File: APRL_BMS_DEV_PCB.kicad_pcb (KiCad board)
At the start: 4 copper layers, 2 parts, among them U1 BQ756506-Q1, U2 STM32F446RCTx

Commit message: Edited PCB a little
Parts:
- added C1: 1u, Capacitor_SMD:C_0603_1608Metric, F.Cu at (80.2, 61.4)
- added C10: 10n, Capacitor_SMD:C_0603_1608Metric, F.Cu at (80.2, 84.0)
- added C11: 1u, Capacitor_SMD:C_0603_1608Metric, F.Cu at (84.2, 61.4)
- added C12: 4.7u, Capacitor_SMD:C_0603_1608Metric, F.Cu at (84.2, 63.9)
- added C13: 20n, Capacitor_SMD:C_0603_1608Metric, F.Cu at (84.2, 66.5)
- added C14: .47u, Capacitor_SMD:C_0603_1608Metric, F.Cu at (84.2, 69.0)
- added C15: 0.1u, Capacitor_SMD:C_0603_1608Metric, F.Cu at (84.2, 71.5)
- added C16: 0.2u, Capacitor_SMD:C_0603_1608Metric, F.Cu at (134.7, 44.5)
- added C17: .56u, Capacitor_SMD:C_0603_1608Metric, F.Cu at (84.2, 74.0)
- added C18: 10u, Capacitor_SMD:C_0603_1608Metric, F.Cu at (84.2, 76.5)
- added C19: 1.5u, Capacitor_SMD:C_0603_1608Metric, F.Cu at (134.7, 47.0)
- added C2: 100n, Capacitor_SMD:C_0603_1608Metric, F.Cu at (80.2, 63.9)
- added C20: 1.5u, Capacitor_SMD:C_0603_1608Metric, F.Cu at (134.7, 49.5)
- added C21: 1.5u, Capacitor_SMD:C_0603_1608Metric, F.Cu at (134.7, 52.0)
- added C22: 1.5u, Capacitor_SMD:C_0603_1608Metric, F.Cu at (134.7, 54.5)
- added C23: 1.5u, Capacitor_SMD:C_0603_1608Metric, F.Cu at (134.7, 57.0)
- added C24: 1.5u, Capacitor_SMD:C_0603_1608Metric, F.Cu at (138.7, 44.5)
- added C25: 1.5u, Capacitor_SMD:C_0603_1608Metric, F.Cu at (84.2, 79.0)
- added C26: 1.5u, Capacitor_SMD:C_0603_1608Metric, F.Cu at (84.2, 81.5)
- added C27: 1.5u, Capacitor_SMD:C_0603_1608Metric, F.Cu at (84.2, 84.0)
- added C28: 1.5u, Capacitor_SMD:C_0603_1608Metric, F.Cu at (88.2, 61.4)
- added C29: 1.5u, Capacitor_SMD:C_0603_1608Metric, F.Cu at (88.2, 63.9)
- added C3: 30p, Capacitor_SMD:C_0603_1608Metric, F.Cu at (80.2, 66.5)
- added C30: 1.5u, Capacitor_SMD:C_0603_1608Metric, F.Cu at (88.2, 66.5)
- added C31: 1.5u, Capacitor_SMD:C_0603_1608Metric, F.Cu at (138.7, 47.0)
- added C32: 1.5u, Capacitor_SMD:C_0603_1608Metric, F.Cu at (88.2, 69.0)
- added C33: 2.2u, Capacitor_SMD:C_0603_1608Metric, F.Cu at (88.2, 71.5)
- added C34: 2.2u, Capacitor_SMD:C_0603_1608Metric, F.Cu at (88.2, 74.0)
- added C35: 1u, Capacitor_SMD:C_0603_1608Metric, F.Cu at (88.2, 76.5)
- added C36: 0.1u, Capacitor_SMD:C_0603_1608Metric, F.Cu at (138.7, 49.5)
- added C37: 0.1u, Capacitor_SMD:C_0603_1608Metric, F.Cu at (138.7, 52.0)
- added C4: 30p, Capacitor_SMD:C_0603_1608Metric, F.Cu at (80.2, 69.0)
- added C5: 10u, Capacitor_SMD:C_0603_1608Metric, F.Cu at (80.2, 71.5)
- added C6: 100n, Capacitor_SMD:C_0603_1608Metric, F.Cu at (80.2, 74.0)
- added C7: 100n, Capacitor_SMD:C_0603_1608Metric, F.Cu at (80.2, 76.5)
- added C8: 100n, Capacitor_SMD:C_0603_1608Metric, F.Cu at (80.2, 79.0)
- added C9: 100n, Capacitor_SMD:C_0603_1608Metric, F.Cu at (167.0, 97.0)
- added D1: RED, LED_SMD:LED_0603_1608Metric, F.Cu at (134.8, 64.2)
- added FB1: 120R, Resistor_SMD:R_0603_1608Metric, F.Cu at (138.7, 54.5)
- added J1: Conn_01x04_Pin, Connector_PinHeader_2.54mm:PinHeader_1x04_P2.54mm_Vertical, F.Cu at (180.0, 98.5)
- added J2: Conn_01x02_Pin, Connector_PinHeader_2.54mm:PinHeader_1x02_P2.54mm_Vertical, F.Cu at (147.6, 57.6)
- added J3: Conn_01x02_Pin, Connector_PinHeader_2.54mm:PinHeader_1x02_P2.54mm_Vertical, F.Cu at (152.2, 57.6)
- added J4: Conn_01x08_Pin, Connector_PinHeader_2.54mm:PinHeader_1x08_P2.54mm_Vertical, F.Cu at (120.9, 92.5)
- added J5: Conn_01x01_Pin, Connector_PinHeader_2.54mm:PinHeader_1x01_P2.54mm_Vertical, F.Cu at (135.0, 60.6)
- added Q1: Q_NPN, Package_TO_SOT_SMD:SOT-223, F.Cu at (109.5, 62.5)
- added R1: 10K, Resistor_SMD:R_0603_1608Metric, F.Cu at (88.2, 79.0)
- added R10: 100, Resistor_SMD:R_0603_1608Metric, F.Cu at (92.2, 74.0)
- added R11: 100, Resistor_SMD:R_0603_1608Metric, F.Cu at (92.2, 76.5)
- added R12: 100, Resistor_SMD:R_0603_1608Metric, F.Cu at (92.2, 79.0)
- added R13: 100, Resistor_SMD:R_0603_1608Metric, F.Cu at (92.2, 81.5)
- added R14: 100, Resistor_SMD:R_0603_1608Metric, F.Cu at (92.2, 84.0)
- added R15: 6.2, Resistor_SMD:R_0603_1608Metric, F.Cu at (96.2, 61.4)
- added R16: 100, Resistor_SMD:R_0603_1608Metric, F.Cu at (96.2, 63.9)
- added R17: 30, Resistor_SMD:R_0603_1608Metric, F.Cu at (96.2, 66.5)
- added R18: 400, Resistor_SMD:R_0603_1608Metric, F.Cu at (96.2, 69.0)
- added R19: 500, Resistor_SMD:R_0603_1608Metric, F.Cu at (96.2, 71.5)
- added R2: 1.2K, Resistor_SMD:R_0603_1608Metric, F.Cu at (100.3, 69.8)
- added R20: 10, Resistor_SMD:R_0603_1608Metric, F.Cu at (96.2, 74.0)
- added R21: 100k, Resistor_SMD:R_0603_1608Metric, F.Cu at (96.2, 76.5)
- added R22: 100k, Resistor_SMD:R_0603_1608Metric, F.Cu at (96.2, 79.0)
- added R23: 4.7k, Resistor_SMD:R_0603_1608Metric, F.Cu at (96.2, 81.5)
- added R3: 6.2, Resistor_SMD:R_0603_1608Metric, F.Cu at (88.2, 81.5)
- added R4: 6.2, Resistor_SMD:R_0603_1608Metric, F.Cu at (88.2, 84.0)
- added R5: 6.2, Resistor_SMD:R_0603_1608Metric, F.Cu at (92.2, 61.4)
- added R6: 6.2, Resistor_SMD:R_0603_1608Metric, F.Cu at (92.2, 63.9)
- added R7: 6.2, Resistor_SMD:R_0603_1608Metric, F.Cu at (92.2, 66.5)
- added R8: 6.2, Resistor_SMD:R_0603_1608Metric, F.Cu at (92.2, 69.0)
- added R9: 100, Resistor_SMD:R_0603_1608Metric, F.Cu at (92.2, 71.5)
- added U3: ISO7741DWR, Package_SO:SOIC-16W_5.3x10.2mm_P1.27mm, F.Cu at (139.8, 103.6)
- added Y1: 20MHz, Crystal:Crystal_SMD_3225-4Pin_3.2x2.5mm, F.Cu at (159.0, 103.5)
- moved U2 53.2 mm to (171.4, 105.3)
- moved U1 22.3 mm to (110.5, 105.0), turned to -90 degrees
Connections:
- U1 pad 1: unconnected-(U1-BAT-Pad1) -> /BAT
- U1 pad 22: unconnected-(U1-CB6-Pad22) -> /CB6
- U1 pad 23: unconnected-(U1-VC6-Pad23) -> /VC6
- U1 pad 24: unconnected-(U1-CB5-Pad24) -> /CB5
- U1 pad 25: unconnected-(U1-VC5-Pad25) -> /VC5
- U1 pad 26: unconnected-(U1-CB4-Pad26) -> /CB4
- U1 pad 27: unconnected-(U1-VC4-Pad27) -> /VC4
- U1 pad 28: unconnected-(U1-CB3-Pad28) -> /CB3
- U1 pad 29: unconnected-(U1-VC3-Pad29) -> /VC3
- U1 pad 30: unconnected-(U1-CB2-Pad30) -> /CB2
- U1 pad 31: unconnected-(U1-VC2-Pad31) -> /VC2
- U1 pad 32: unconnected-(U1-CB1-Pad32) -> /CB1
- U1 pad 33: unconnected-(U1-VC1-Pad33) -> /VC1
- U1 pad 34: unconnected-(U1-CB0-Pad34) -> /CB0
- U1 pad 35: unconnected-(U1-VC0-Pad35) -> /VC0
- U1 pad 37: unconnected-(U1-REFHP-Pad37) -> /REFHP
- U1 pad 38: unconnected-(U1-AVDD-Pad38) -> /AVDD
- U1 pad 44: unconnected-(U1-NEG5V-Pad44) -> Net-(U1-NEG5V)
- U1 pad 45: unconnected-(U1-CVDD-Pad45) -> /CVDD
- U1 pad 47: unconnected-(U1-LDOIN-Pad47) -> /LDOIN
- U1 pad 48: unconnected-(U1-NPNB-Pad48) -> /NPNB
- U1 pad 49: unconnected-(U1-DVDD-Pad49) -> /DVDD
- U1 pad 51: unconnected-(U1-TSREF-Pad51) -> Net-(J5-Pin_1)
- U1 pad 52: unconnected-(U1-RX-Pad52) -> /RX_BMS
- U1 pad 53: unconnected-(U1-TX-Pad53) -> /TX_BMS
- U1 pad 54: unconnected-(U1-GPIO8-Pad54) -> /GPIO1
- U1 pad 55: unconnected-(U1-GPIO7-Pad55) -> /GPIO2
- U1 pad 56: unconnected-(U1-GPIO6-Pad56) -> /GPIO3
- U1 pad 57: unconnected-(U1-GPIO5-Pad57) -> /GPIO4
- U1 pad 58: unconnected-(U1-GPIO4-Pad58) -> /GPIO5
- U1 pad 59: unconnected-(U1-GPIO3-Pad59) -> /GPIO6
- U1 pad 60: unconnected-(U1-GPIO2-Pad60) -> /GPIO7
- U1 pad 61: unconnected-(U1-GPIO1-Pad61) -> /GPIO8
- U1 pad 62: unconnected-(U1-NFAULT-Pad62) -> /NFAULT
- U1 pad 63: unconnected-(U1-SRN-Pad63) -> GND
- U1 pad 64: unconnected-(U1-SRP-Pad64) -> /CELL_0
- U2 pad 30: unconnected-(U2-VCAP_1-Pad30) -> Net-(U2-VCAP_1)
- U2 pad 39: unconnected-(U2-PC8-Pad39) -> /NFAULT_IN
- U2 pad 5: Net-(U2-PH0) -> /OSC_IN
- U2 pad 6: Net-(U2-PH1) -> /OSC_OUT

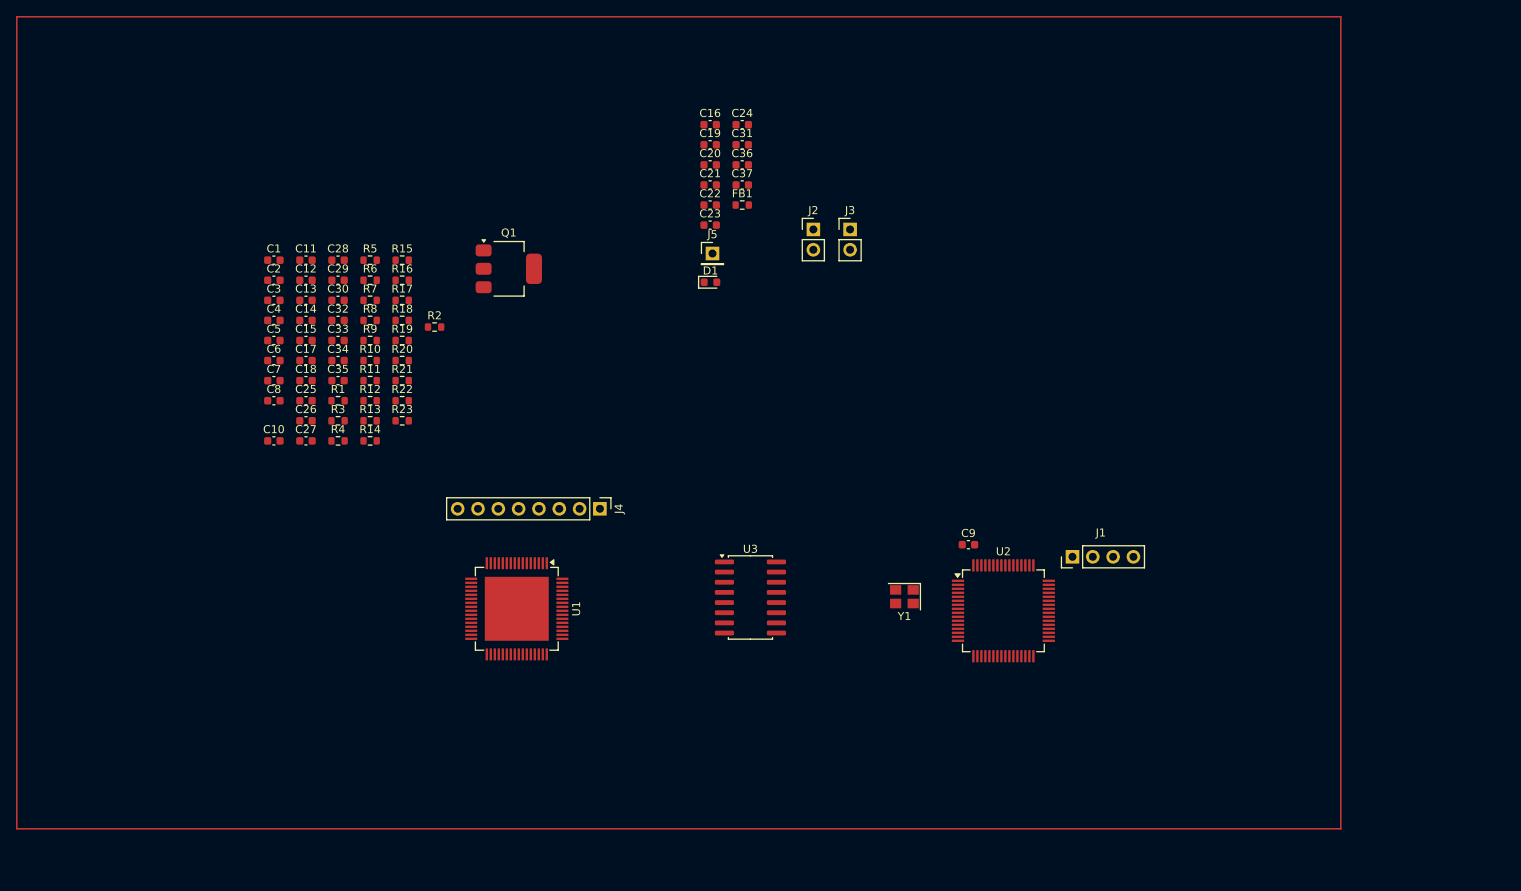
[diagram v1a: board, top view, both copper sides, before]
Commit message: Added PCB Traces, fixed Digital Isolator
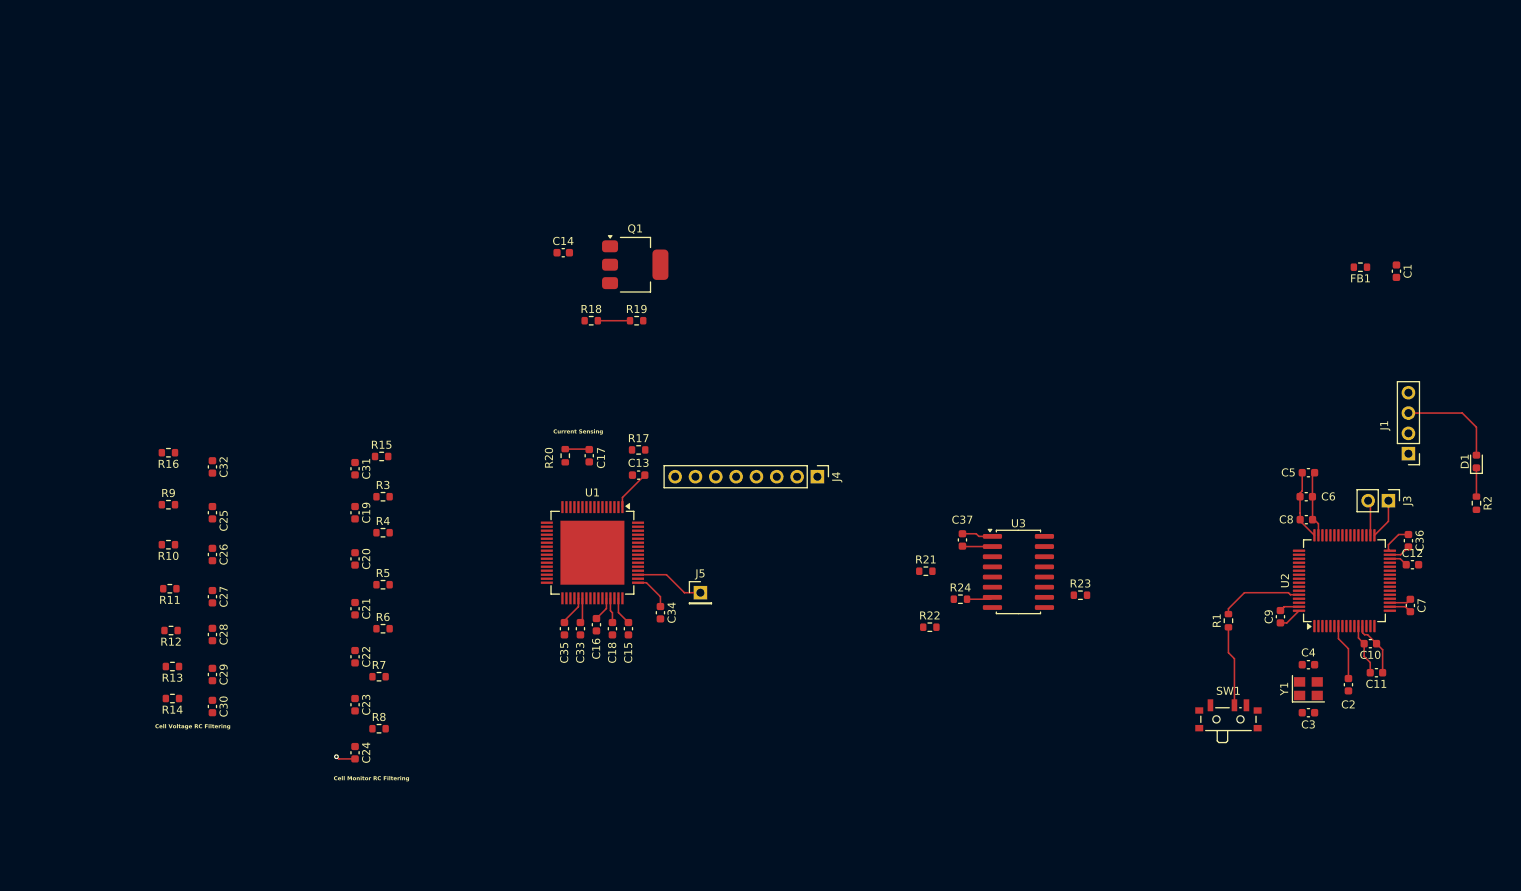
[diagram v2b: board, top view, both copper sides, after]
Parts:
- removed J2: Conn_01x02_Pin, Connector_PinHeader_2.54mm:PinHeader_1x02_P2.54mm_Vertical
- added R24: 4.7k, Resistor_SMD:R_0603_1608Metric, F.Cu at (166.0, 103.8)
- added SW1: SW_SPDT, Button_Switch_SMD:SW_SPDT_PCM12, F.Cu at (199.5, 118.5)
- moved C7 144.8 mm to (222.2, 104.6), turned to -90 degrees
- moved C2 143.5 mm to (214.5, 114.5), turned to -90 degrees
- moved C11 143.4 mm to (218.0, 113.0), turned to 180 degrees
- moved C12 142.8 mm to (222.5, 99.5)
- moved C1 140.3 mm to (220.5, 62.8), turned to -90 degrees
- moved C10 139.4 mm to (217.2, 109.4), turned to 180 degrees
- moved C3 139.2 mm to (209.5, 118.0)
- moved C4 136.3 mm to (209.5, 112.0), turned to 180 degrees
- moved R2 132.1 mm to (230.5, 91.8), turned to -90 degrees
- moved C5 130.4 mm to (209.5, 88.0)
- moved C6 130.2 mm to (209.2, 91.0)
- moved C8 129.9 mm to (209.2, 93.9)
- moved R1 114.6 mm to (199.5, 106.5), turned to 90 degrees
- moved D1 98.3 mm to (230.5, 86.6), turned to 90 degrees
- moved C36 95.6 mm to (222.0, 96.5), turned to -90 degrees
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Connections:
- net /SWDIO renamed Net-(J1-Pin_1)
- net Net-(J5-Pin_1) renamed /TSREF
- net Net-(U1-NEG5V) renamed /NEG5V
- net Net-(U2-VCAP_1) renamed /VCAP_1
- R21 pad 2: /CVDD -> /RX_BMS
- U2 pad 14: /UART_TX -> unconnected-(U2-PA0-Pad14)
- U2 pad 15: /UART_RX -> unconnected-(U2-PA1-Pad15)
- U2 pad 44: /CAN1_RX -> unconnected-(U2-PA11-Pad44)
- U2 pad 45: /CAN1_TX -> unconnected-(U2-PA12-Pad45)
- U2 pad 51: unconnected-(U2-PC10-Pad51) -> /UART_TX
- U2 pad 52: unconnected-(U2-PC11-Pad52) -> /UART_RX
- U3 pad 11: unconnected-(U3-IND-Pad11) -> /UART_TX
- U3 pad 12: /NFAULT_IN -> unconnected-(U3-OUTC-Pad12)
- U3 pad 14: /UART_TX -> /NFAULT_IN
- U3 pad 3: /RX_BMS -> /NFAULT
- U3 pad 5: /NFAULT -> unconnected-(U3-INC-Pad5)
- U3 pad 6: unconnected-(U3-OUTD-Pad6) -> /RX_BMS
- U3 pad 7: GND -> /EN1
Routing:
- net +3.3V: track 0.00 -> 31.0 mm
- net GND: track 0.00 -> 29.1 mm, vias 0 -> 1
- net /BOOT0: track 0.00 -> 10.4 mm
- net /SW_BOOT0: track 0.00 -> 10.4 mm
- net /TSREF: track 0.00 -> 8.73 mm
- net +3.3VA: track 0.00 -> 7.09 mm
- net /NRST: track 0.00 -> 7.07 mm
- net /CVDD: track 0.00 -> 7.02 mm
- net /BAT: track 0.00 -> 5.16 mm
- net /CAN2_RX: track 0.00 -> 5.05 mm
- net /DVDD: track 0.00 -> 4.75 mm
- net /CAN2_TX: track 0.00 -> 4.45 mm
- net Net-(R18-Pad2): track 0.00 -> 4.03 mm
- net /REFHP: track 0.00 -> 3.79 mm
- net Net-(D1-K): track 0.00 -> 3.60 mm
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- added copper zone on In1.Cu, net GND
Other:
- board text added: "Cell Monitor RC Filtering"
- board text added: "Cell Voltage RC Filtering"
- board text added: "Current Sensing"

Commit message: Refined some traces
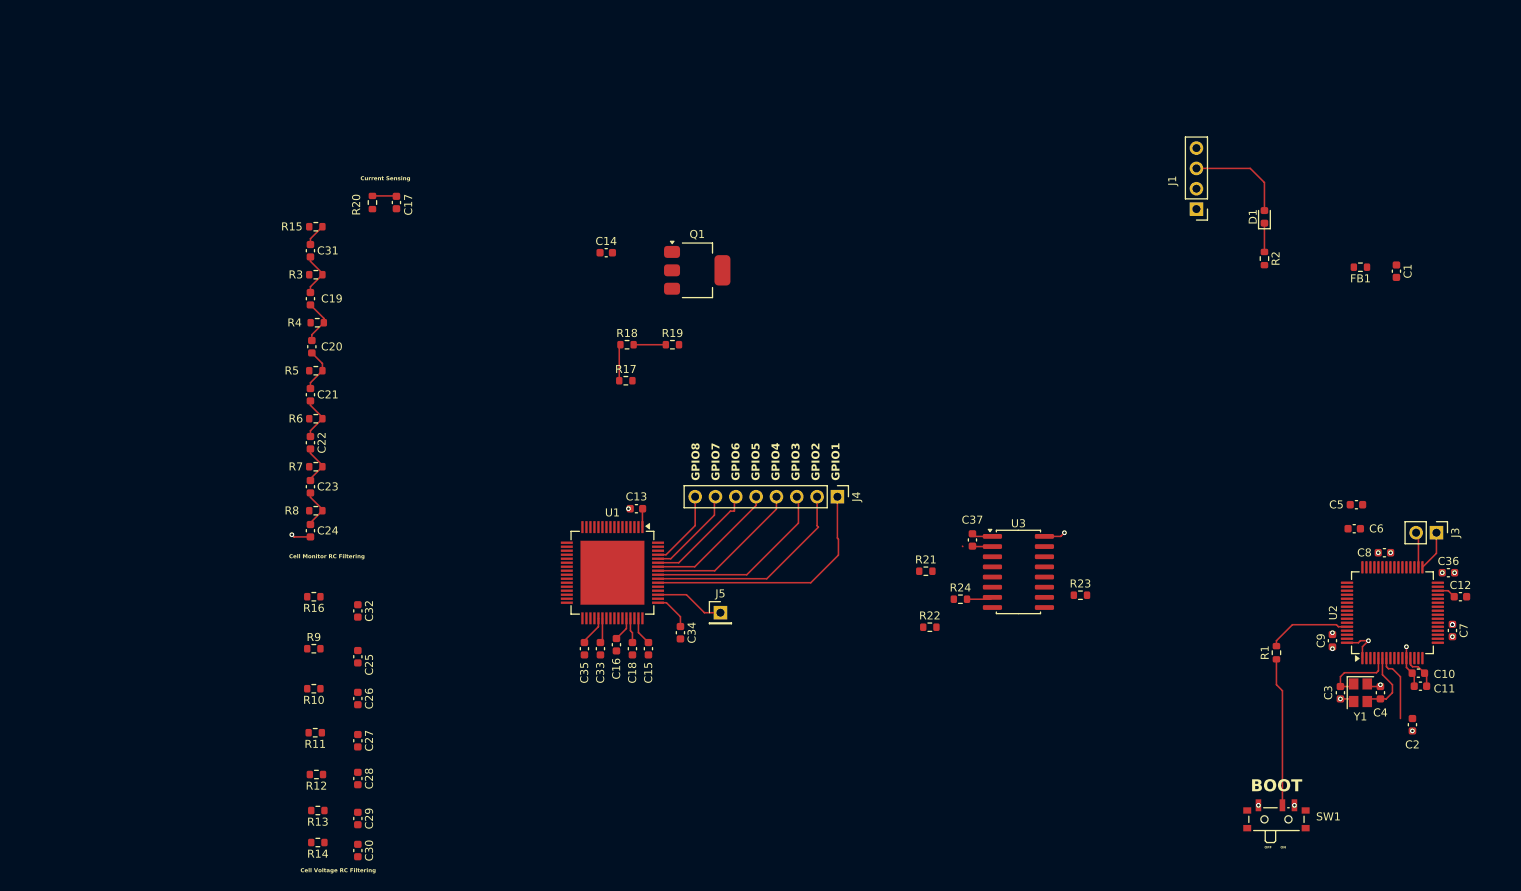
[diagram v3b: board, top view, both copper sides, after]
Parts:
- moved D1 40.5 mm to (204.0, 56.0)
- moved J1 40.5 mm to (195.5, 55.0)
- moved R2 40.5 mm to (204.0, 61.2)
- moved C17 39.8 mm to (95.5, 54.2)
- moved R20 39.8 mm to (92.5, 54.2)
- moved R15 29.9 mm to (85.4, 57.2), turned to 180 degrees
- moved R3 29.0 mm to (85.4, 63.2), turned to 180 degrees
- moved R8 28.4 mm to (85.4, 92.8), turned to 180 degrees
- moved C24 28.3 mm to (84.8, 95.2)
- moved R5 28.0 mm to (85.4, 75.2), turned to 180 degrees
- moved C23 27.8 mm to (84.8, 89.8)
- moved C31 27.8 mm to (84.8, 60.2)
- moved R6 27.6 mm to (85.4, 81.2), turned to 180 degrees
- moved R4 27.5 mm to (85.6, 69.2), turned to 180 degrees
- moved R7 27.4 mm to (85.4, 87.2), turned to 180 degrees
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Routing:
- net /GPIO1: track 0.00 -> 31.3 mm
- net /GPIO2: track 0.00 -> 26.6 mm
- net /GPIO3: track 0.00 -> 23.6 mm
- net /GPIO4: track 0.00 -> 19.5 mm
- net /GPIO5: track 0.00 -> 16.5 mm
- net /GPIO6: track 0.00 -> 14.1 mm
- net GND: track 29.1 -> 15.8 mm, vias 1 -> 11
- net /GPIO7: track 0.00 -> 11.7 mm
- net /GPIO8: track 0.00 -> 9.76 mm
- net +3.3V: track 31.0 -> 21.4 mm, vias 0 -> 8
- net /OSC_IN: track 0.14 -> 9.65 mm
- net /SW_BOOT0: track 10.4 -> 18.9 mm
- net /OSC_OUT: track 0.00 -> 8.45 mm
- net /CB4: track 0.00 -> 5.77 mm
- net /CB5: track 0.00 -> 5.69 mm
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- added copper zone on In2.Cu, net +3.3V
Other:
- board text added: "BOOT"
- board text added: "GPIO1"
- board text added: "GPIO2"
- board text added: "GPIO3"
- board text added: "GPIO4"
- board text added: "GPIO5"
- board text added: "GPIO6"
- board text added: "GPIO7"
- board text added: "GPIO8"
- board text added: "OFF"
- board text added: "ON"
